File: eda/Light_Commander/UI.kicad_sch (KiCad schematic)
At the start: 7 parts, among them SW1 RotaryEncoder_Switch

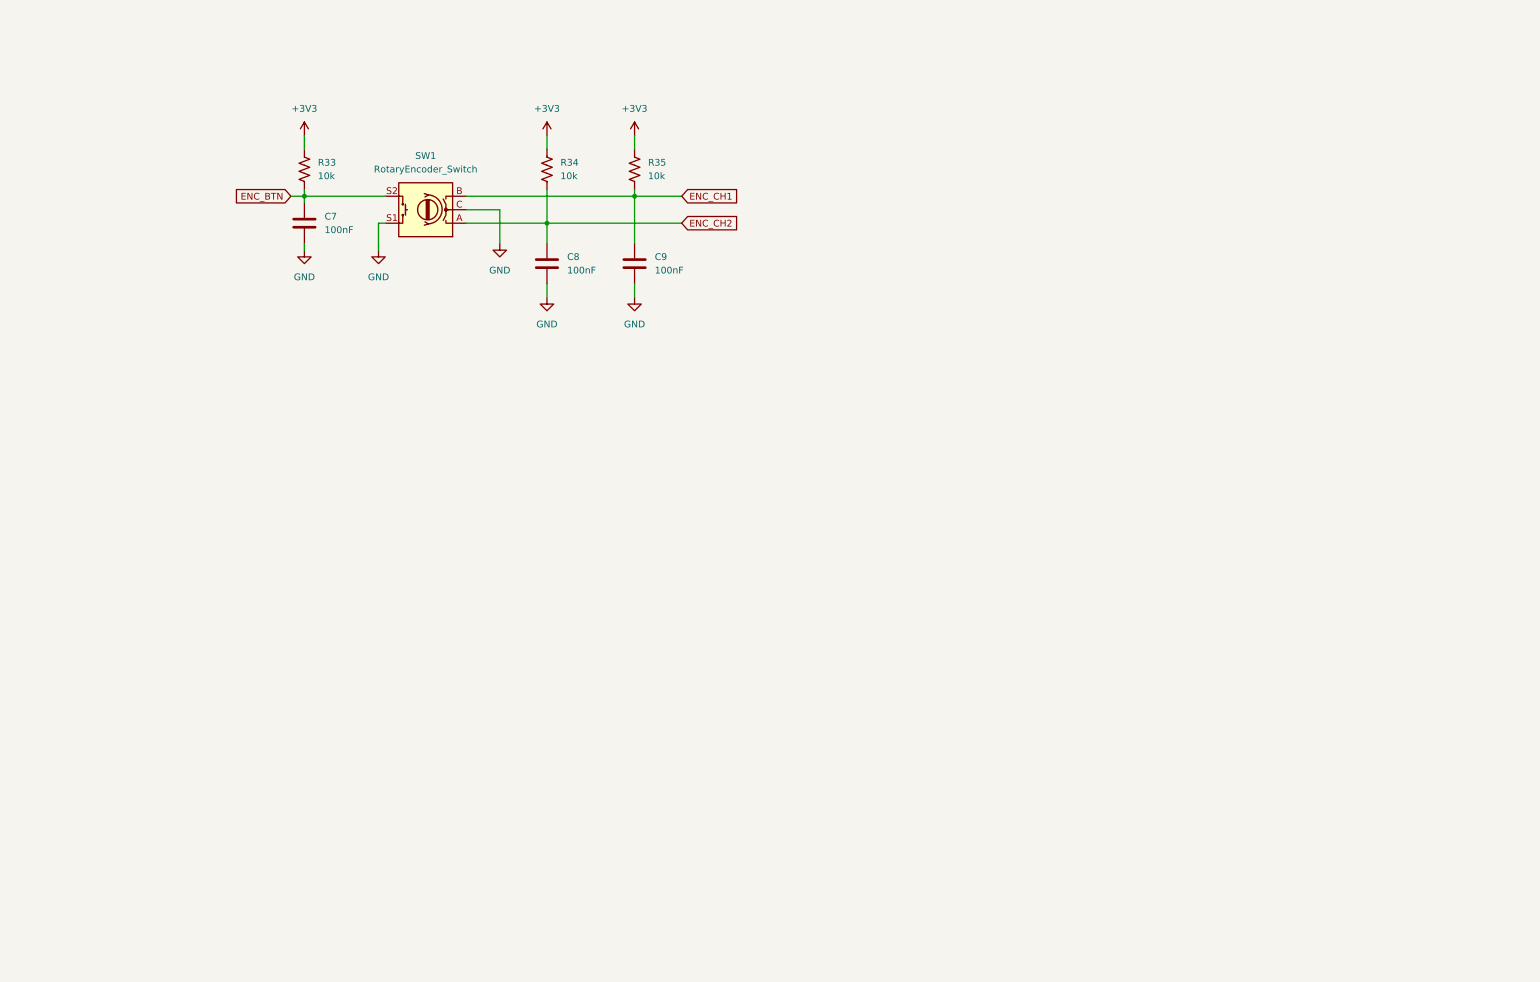
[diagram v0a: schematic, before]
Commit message: Add MDI in and thru to schematic
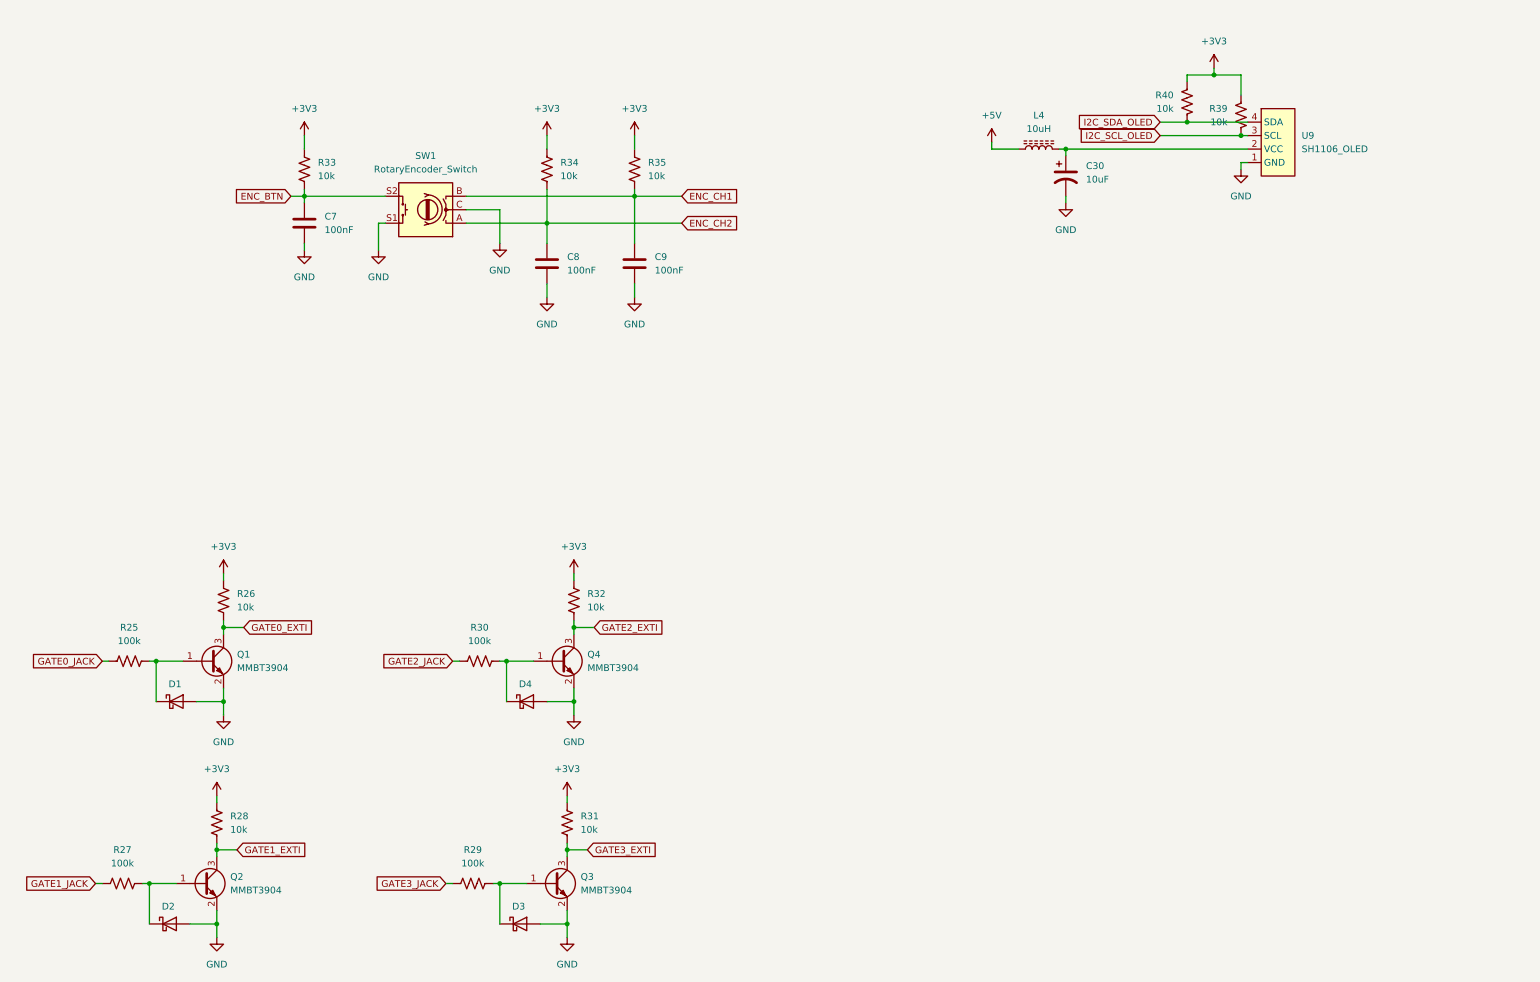
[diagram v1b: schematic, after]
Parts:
- added C30: 10uF, Capacitor_SMD:C_Elec_6.3x7.7, symbol Device:C_Polarized_US
- added D1, D2, D3, D4: GSBAT54W, Diode_SMD:D_SOD-123, symbol Device:D_Schottky
- added L4: 10uH, Inductor_SMD:L_1210_3225Metric, symbol Device:L_Ferrite
- added Q1, Q2, Q3, Q4: MMBT3904, Package_TO_SOT_SMD:SOT-23, symbol Transistor_BJT:MMBT3904
- added R25, R27, R29, R30: 100k, Resistor_SMD:R_0805_2012Metric, symbol Device:R_US
- added R26, R28, R31, R32, R39, R40: 10k, Resistor_SMD:R_0805_2012Metric, symbol Device:R_US
- added U9: SH1106_OLED, footprints:SH1106_1.3in_OLED, symbol SH1106_OLED:SH1106_OLED
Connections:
- net +3V3: now also R26.1, R28.1, R31.1, R32.1, R39.1, R40.1
- net GND: now also C30.2, D1.2 (A), D2.2 (A), D3.2 (A), D4.2 (A), Q1.2 (E), Q2.2 (E), Q3.2 (E), Q4.2 (E), U9.1 (GND)
- new net: D3.1 (K), Q3.1 (B), R29.2
- new net: D2.1 (K), Q2.1 (B), R27.2
- new net: D4.1 (K), Q4.1 (B), R30.2
- new net: C30.1, L4.2, U9.2 (VCC)
- new net: D1.1 (K), Q1.1 (B), R25.2
- new net +5V: L4.1
- new net GATE0_EXTI: Q1.3 (C), R26.2
- new net GATE0_JACK: R25.1
- new net GATE1_EXTI: Q2.3 (C), R28.2
- new net GATE1_JACK: R27.1
- new net GATE2_EXTI: Q4.3 (C), R32.2
- new net GATE2_JACK: R30.1
- new net GATE3_EXTI: Q3.3 (C), R31.2
- new net GATE3_JACK: R29.1
- new net I2C_SCL_OLED: R39.2, U9.3 (SCL)
- new net I2C_SDA_OLED: R40.2, U9.4 (SDA)

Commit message: Add buttons, SWD, and LED reverse polarity protection to schematic
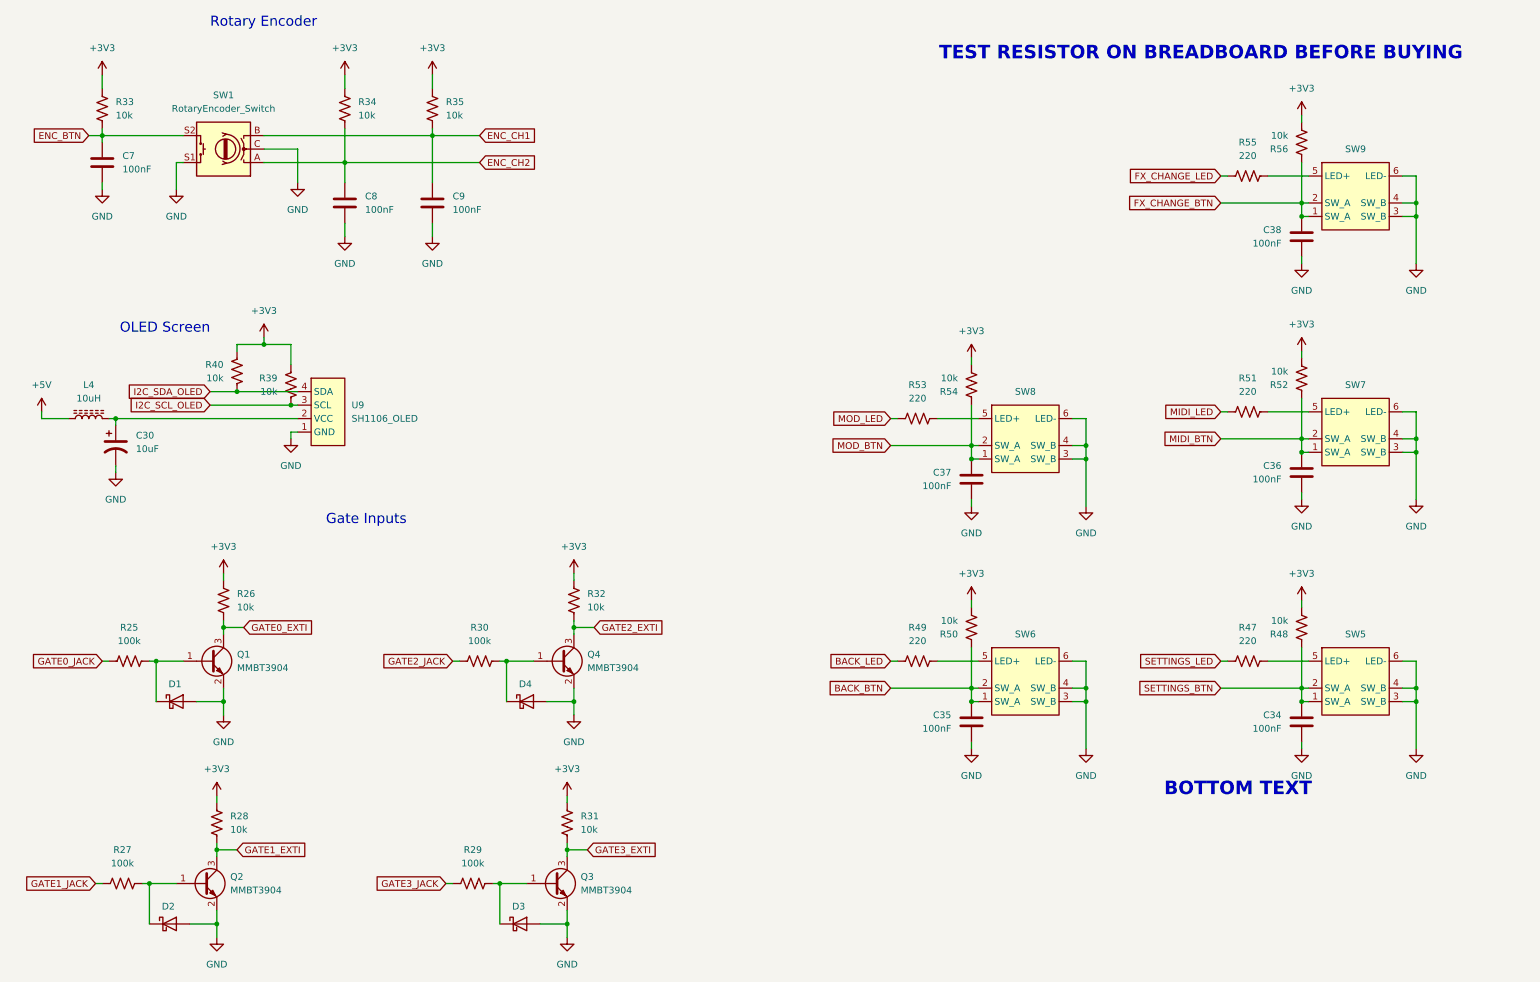
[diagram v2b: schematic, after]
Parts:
- added C34, C35, C36, C37, C38: 100nF, Capacitor_SMD:C_0805_2012Metric, symbol Device:C
- added R47, R49, R51, R53, R55: 220, Resistor_SMD:R_0805_2012Metric, symbol Device:R_US
- added R48, R50, R52, R54, R56: 10k, Resistor_SMD:R_0805_2012Metric, symbol Device:R_US
- added SW5, SW6, SW7, SW8, SW9: (no value), footprints:SW_Tact_Low_Profile_LED_ExtraHoles, symbol SW_Tact_Low_Profile_LED_ExtraHoles:SW_Tact_Low_Profile_LED_ExtraHoles
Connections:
- net +3V3: now also R48.2, R50.2, R52.2, R54.2, R56.2
- net GND: now also C34.2, C35.2, C36.2, C37.2, C38.2, SW5.3 (SW_B), SW5.4 (SW_B), SW5.6 (LED-), SW6.3 (SW_B), SW6.4 (SW_B), SW6.6 (LED-), SW7.3 (SW_B), SW7.4 (SW_B), SW7.6 (LED-), SW8.3 (SW_B), SW8.4 (SW_B), SW8.6 (LED-), SW9.3 (SW_B), SW9.4 (SW_B), SW9.6 (LED-)
- new net: R49.1, SW6.5 (LED+)
- new net: R53.1, SW8.5 (LED+)
- new net: R55.1, SW9.5 (LED+)
- new net: R47.1, SW5.5 (LED+)
- new net: R51.1, SW7.5 (LED+)
- new net BACK_BTN: C35.1, R50.1, SW6.1 (SW_A), SW6.2 (SW_A)
- new net BACK_LED: R49.2
- new net FX_CHANGE_BTN: C38.1, R56.1, SW9.1 (SW_A), SW9.2 (SW_A)
- new net FX_CHANGE_LED: R55.2
- new net MIDI_BTN: C36.1, R52.1, SW7.1 (SW_A), SW7.2 (SW_A)
- new net MIDI_LED: R51.2
- new net MOD_BTN: C37.1, R54.1, SW8.1 (SW_A), SW8.2 (SW_A)
- new net MOD_LED: R53.2
- new net SETTINGS_BTN: C34.1, R48.1, SW5.1 (SW_A), SW5.2 (SW_A)
- new net SETTINGS_LED: R47.2
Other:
- note added: "BOTTOM TEXT"
- note added: "Gate Inputs"
- note added: "OLED Screen"
- note added: "Rotary Encoder"
- note added: "TEST RESISTOR ON BREADBOARD BEFORE BUYING"
- moved on the sheet: C30, C7, C8, C9, L4, R33, R34, R35, R39, R40, SW1, U9

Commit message: Start of PCB
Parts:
- SW1: Digikey_PN (none) -> PEC11R-4220K-S0024-ND
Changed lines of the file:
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@@
+			)
+		)
+		(property "Digikey_PN" "PEC11R-4220K-S0024-ND"
+			(at 52.07 41.91 0)
+			(hide yes)
+			(show_name no)
+			(do_not_autoplace no)
+			(effects
+				(font
+					(size 1.27 1.27)
+				)
 			)
 		)

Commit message: Start of trace routing
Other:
- note added: "TEST RESISTOR ON BREADBOARD BEFORE BUYING 200 ohm at 3.3V looks good to me!"
- note removed: "TEST RESISTOR ON BREADBOARD BEFORE BUYING"
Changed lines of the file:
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@@
 		)
 	)
-	(text "TEST RESISTOR ON BREADBOARD BEFORE BUYING"
+	(text "TEST RESISTOR ON BREADBOARD BEFORE BUYING\n\n200 ohm at 3.3V looks good to me!"
 		(exclude_from_sim no)
 		(at 186.944 23.876 0)
